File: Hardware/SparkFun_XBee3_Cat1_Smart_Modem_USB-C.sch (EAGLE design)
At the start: 53 parts, among them J4 QWIIC_RIGHT_ANGLE, U2 AP63203, U5 ESD Diode, U6 CP210X

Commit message: Moves parts around
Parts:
- removed FRAME2: FRAME-LETTER, SparkFun-Aesthetics:FRAME-LETTER
- added FRAME1: FRAME-LEDGER, SparkFun-Aesthetics:FRAME-LEDGER
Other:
- moved on the sheet: ALED, C1, C10, C2, C3, C4, C5, C6, C7, C8, C9, D2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

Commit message: Routes board
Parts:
- J3: value (none) -> USB Female Type C Connector; device SparkFun-Connectors:USB_C_2-LAYER_PADS -> SparkFun-Connectors:USB_C_4-LAYER-ISOLATED
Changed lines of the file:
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@@
 <part name="GND17" library="SparkFun-PowerSymbols" deviceset="GND" device=""/>
 <part name="J7" library="SparkFun-Connectors" deviceset="CONN_02" device="1X02_NO_SILK"/>
-<part name="J3" library="SparkFun-Connectors" deviceset="USB_C" device="_2-LAYER_PADS"/>
+<part name="J3" library="SparkFun-Connectors" deviceset="USB_C" device="_4-LAYER-ISOLATED" value="USB Female Type C Connector"/>
 <part name="GND4" library="SparkFun-PowerSymbols" deviceset="GND" device=""/>
 <part name="R7" library="SparkFun-Resistors" deviceset="5.1KOHM" device="5.1KOHM-0603-1/10W-1%" value="5.1k"/>

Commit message: Commits (finally) to shrinking the LED resistors so that I can fit in labels
* Increases schematic frame size to Ledger
* Adds measures
* Adds additional silk
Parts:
- LOGO3: value QWIIC_LOGO_5MM -> QWIIC_LOGO_3MM; device SparkFun-Aesthetics:QWIIC_LOGO_5MM -> SparkFun-Aesthetics:QWIIC_LOGO_3MM
- R11: device SparkFun-Resistors:1KOHM-0603-1/10W-1% -> SparkFun-Resistors:1KOHM-0402T-1/16W-1%
- R12, R2: device SparkFun-Resistors:2.2KOHM-0603-1/10W-1% -> SparkFun-Resistors:2.2KOHM-0402T-1/16W-1%
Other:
- note added: "Cut SHLD jumper to disconnect USB Shield from Ground."
- note added: "USB to UART - CP2104/2N"
- note added: "USB-C"
- note removed: "Cut SHLD/SHLD1 jumper to disconnect USB Shields from Ground."
- moved on the sheet: ALED, C1, C10, C2, C3, C4, C5, C6, C7, C8, C9, D2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

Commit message: Replaces UART IC
* Cuts back ground pour to make room for smaller modules RF singnals
* Fixes polygons
* Adds yellow LED
* Adds additional decoupling caps for RF board
* Increases the size of the board by 0.1" to make space for decoupling caps
* Updates the inductor for switching regulator
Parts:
- removed J7: (no value), SparkFun-Connectors:CONN_021X02_NO_SILK
- removed R17: 22k, SparkFun-Resistors:22KOHM-0603-1/10W-1%
- removed R18: 33k, SparkFun-Resistors:33KOHM-0603-1/10W-1%
- removed R9: 10k, SparkFun-Resistors:10KOHM-0603-1/10W-1%
- removed U6: CP210X, SparkFun-IC-Comms:CP2102N
- added C11, C14: 0.1uF, SparkFun-Capacitors:0.1UF-0603-25V-(+80/-20%)
- added J1, J8: (no value), SparkFun-Connectors:CONN_01PTH_NO_SILK_STAND
- added JP1: (no value), SparkFun-RF:XBEESMD
- added U7: FT231XS, SparkFun-IC-Comms:FT231XS
- C5: value 0.1uF -> 47pF; device SparkFun-Capacitors:0.1UF-0603-25V-(+80/-20%) -> SparkFun-Capacitors:47PF-0603-50V-5%
- C8: value 4.7uF -> 10pF; device SparkFun-Capacitors:4.7UF-0603-6.3V-(10%) -> SparkFun-Capacitors:10PF-0603-50V-5%
- D2: value RED -> Red; device SparkFun-LED:LED-RED0603 -> SparkFun-LED:LED-RED-0603-WE
- D4: value BLUE -> Yellow; device SparkFun-LED:LED-BLUE0603 -> SparkFun-LED:LED-YELLOW0603
- L1: value 4.7μH -> 3.9UH; device SparkFun-Coils:4.7μH_SHIELDED_INDUCTORNPIS_LS -> SparkFun-Coils:3.9UH
- R11: value 1k -> 4.7k; device SparkFun-Resistors:1KOHM-0402T-1/16W-1% -> SparkFun-Resistors:4.7KOHM-0402T-1/16W-1%
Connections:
- removed net N$10: R17.1, R18.2, U6.VBUS
- removed net N$4: J2.D-
- removed net N$9: R9.2, U6.!RSTB
- net 3.3V: now also C11.1, C14.1, U7.!RESET, U7.3V3OUT, U7.VCC, U7.VCCIO; no longer R9.1, U6.VDD, U6.VIO, U6.VREGIN
- net D+: now also U7.USBDP; no longer U6.D+
- net D-: now also U7.USBDM; no longer U6.D-
- net D13/TXO: now also U7.RXD; no longer U6.RXD
- net D14/RXI: now also U7.TXD; no longer U6.TXD
- net D6/!RTS!: now also U7.!RTS; no longer U6.RTS
- net D7/!CTS!: now also U7.!CTS
- net D8/!DTR!: now also U7.!DTR; no longer U6.DTR
- net EN: now also J8.1; no longer J7.1
- net GND: now also C11.2, C14.2, U7.GND@16, U7.GND@6; no longer R18.1, U6.GND
- net VIN: now also J1.1; no longer J7.2, R17.2
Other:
- note added: "RF Module - XBee 3"
- note added: "USB to UART - FT231XS"
- note removed: "RF Module - XBee 3 Cat 1 Smart Modem"
- note removed: "USB to UART - CP2104/2N"
- moved on the sheet: C5, C7, C8, C9

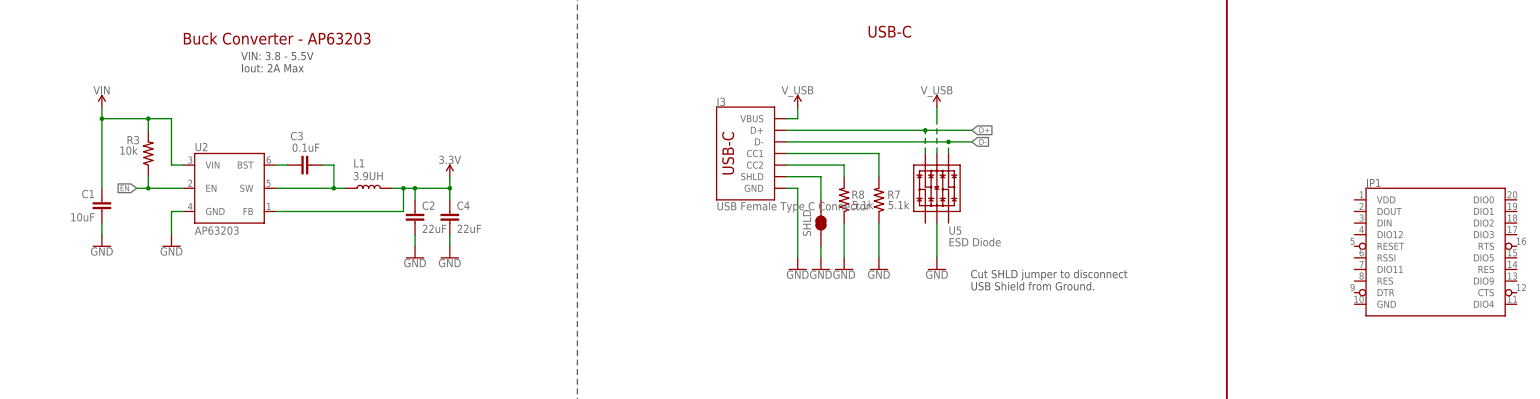
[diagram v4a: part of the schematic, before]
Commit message: Routes some airwires
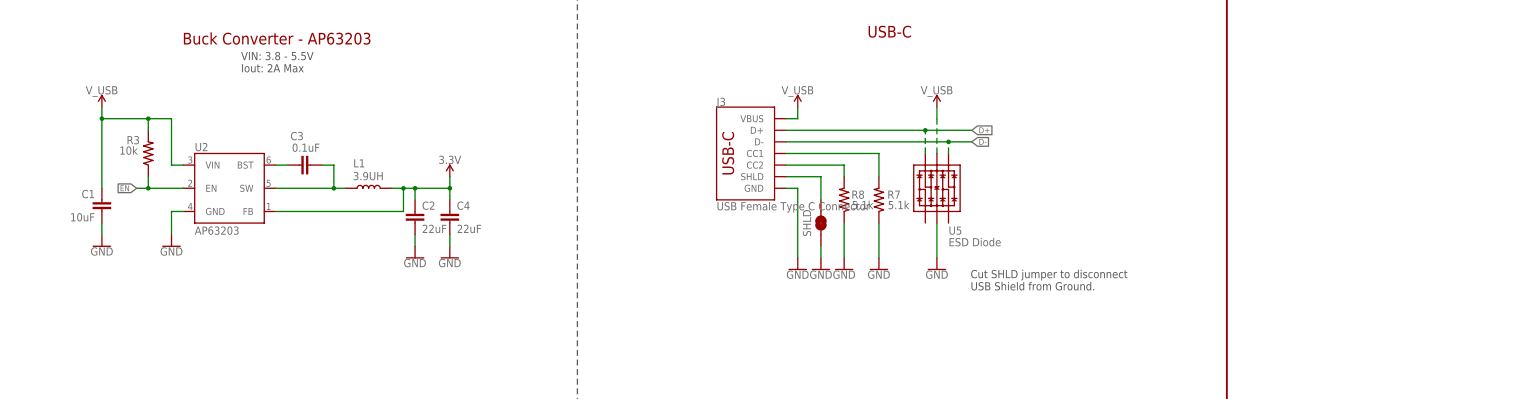
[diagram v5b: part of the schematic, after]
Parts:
- removed JP1: (no value), SparkFun-RF:XBEESMD
- J2: device xbee_smart_modem:XBEE_UPDATEXBEE_SMD_SILK -> xbee_smart_modem:XBEE_UPDATEXBEE_SMD
- R11: device SparkFun-Resistors:4.7KOHM-0402T-1/16W-1% -> SparkFun-Resistors:4.7KOHM-0603-1/10W-1%
- R12, R2: device SparkFun-Resistors:2.2KOHM-0402T-1/16W-1% -> SparkFun-Resistors:2.2KOHM-0603-1/10W-1%
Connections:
- net VIN: no longer C1.1, R3.2, U2.VIN
- net V_USB: now also C1.1, R3.2, U2.VIN

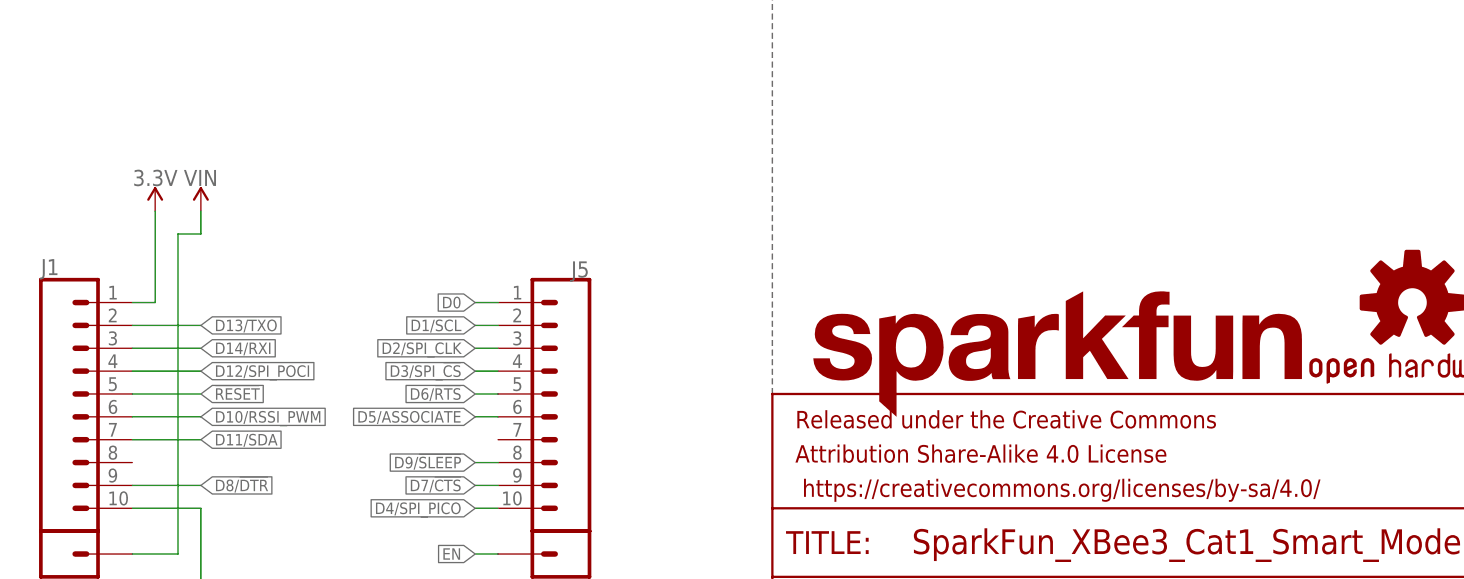
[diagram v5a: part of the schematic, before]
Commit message: Finishes routing airwires, fixes silk
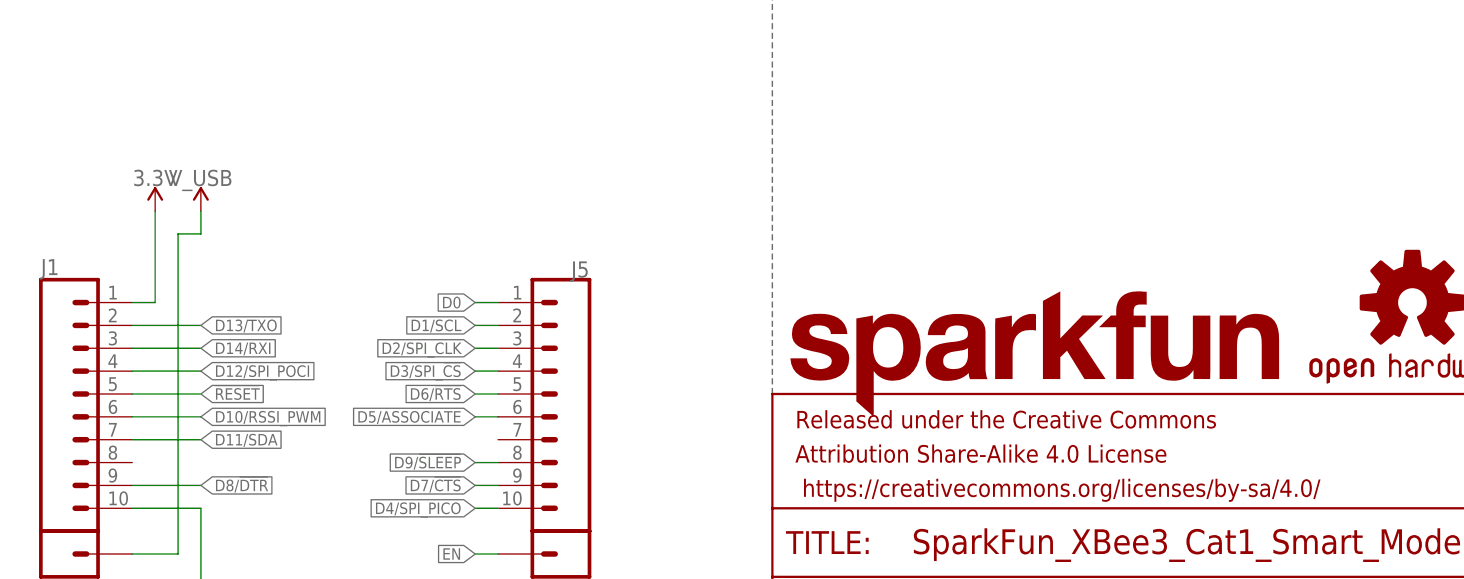
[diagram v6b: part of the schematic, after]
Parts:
- LOGO1: value SFE_LOGO_NAME.1_INCH -> SFE_LOGO_NAME.2_INCH; device SparkFun-Aesthetics:SFE_LOGO_NAME.1_INCH -> SparkFun-Aesthetics:SFE_LOGO_NAME.2_INCH
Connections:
- removed net VIN: J1.1
- net V_USB: now also J1.1
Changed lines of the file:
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@@
 <part name="PLED" library="SparkFun-Jumpers" deviceset="JUMPER-SMT_2_NC_TRACE" device="_SILK" package3d_urn="urn:adsk.eagle:package:39281/1"/>
 <part name="ALED" library="SparkFun-Jumpers" deviceset="JUMPER-SMT_2_NC_TRACE" device="_SILK" package3d_urn="urn:adsk.eagle:package:39281/1"/>
-<part name="LOGO1" library="SparkFun-Aesthetics" deviceset="SFE_LOGO_NAME" device=".1_INCH" value="SFE_LOGO_NAME.1_INCH"/>
 <part name="LOGO2" library="SparkFun-Aesthetics" deviceset="OSHW-LOGO" device="S"/>
 <part name="LOGO3" library="SparkFun-Aesthetics" deviceset="QWIIC_LOGO" device="_3MM" value="QWIIC_LOGO_3MM"/>
@@
 <part name="J1" library="SparkFun-Connectors" deviceset="CONN_01" device="PTH_NO_SILK_STAND"/>
 <part name="J8" library="SparkFun-Connectors" deviceset="CONN_01" device="PTH_NO_SILK_STAND"/>
-<part name="SUPPLY12" library="SparkFun-PowerSymbols" deviceset="VIN" device=""/>
 <part name="SUPPLY5" library="SparkFun-PowerSymbols" deviceset="V_USB" device=""/>
+<part name="SUPPLY11" library="SparkFun-PowerSymbols" deviceset="V_USB" device=""/>
+<part name="LOGO1" library="SparkFun-Aesthetics" deviceset="SFE_LOGO_NAME" device=".2_INCH"/>
 </parts>
 <sheets>
@@
 <attribute name="NAME" x="187.96" y="93.472" size="1.778" layer="95" font="vector" rot="R180" align="center"/>
 </instance>
-<instance part="LOGO1" gate="G$1" x="332.74" y="33.02" smashed="yes"/>
 <instance part="LOGO2" gate="G$1" x="401.32" y="45.72" smashed="yes"/>
 <instance part="LOGO3" gate="G$1" x="421.64" y="40.64" smashed="yes"/>
@@
 <attribute name="NAME" x="309.88" y="14.732" size="1.778" layer="95" font="vector" rot="R180"/>
 </instance>
-<instance part="SUPPLY12" gate="G$1" x="266.7" y="55.88" smashed="yes">
-<attribute name="VALUE" x="266.7" y="58.674" size="1.778" layer="96" font="vector" align="bottom-center"/>
-</instance>
 <instance part="SUPPLY5" gate="G$1" x="185.42" y="246.38" smashed="yes">
 <attribute name="VALUE" x="185.42" y="249.174" size="1.778" layer="96" font="vector" align="bottom-center"/>
 </instance>
+<instance part="SUPPLY11" gate="G$1" x="266.7" y="55.88" smashed="yes">
+<attribute name="VALUE" x="266.7" y="58.674" size="1.778" layer="96" font="vector" align="bottom-center"/>
+</instance>
+<instance part="LOGO1" gate="G$1" x="330.2" y="33.02" smashed="yes"/>
 </instances>
 <busses>
@@
 </segment>
 </net>
-<net name="VIN" class="0">
-<segment>
-<wire x1="259.08" y1="17.78" x2="264.16" y2="17.78" width="0.1524" layer="91"/>
-<wire x1="264.16" y1="17.78" x2="264.16" y2="53.34" width="0.1524" layer="91"/>
-<pinref part="J1" gate="G$1" pin="1"/>
-<wire x1="264.16" y1="53.34" x2="266.7" y2="53.34" width="0.1524" layer="91"/>
-<wire x1="266.7" y1="53.34" x2="266.7" y2="55.88" width="0.1524" layer="91"/>
-<pinref part="SUPPLY12" gate="G$1" pin="VIN"/>
-</segment>
-</net>
 <net name="N$21" class="0">
 <segment>
@@
 <pinref part="SUPPLY5" gate="G$1" pin="V_USB"/>
 </segment>
-</net>
+<segment>
+<wire x1="259.08" y1="17.78" x2="264.16" y2="17.78" width="0.1524" layer="91"/>
+<wire x1="264.16" y1="17.78" x2="264.16" y2="53.34" width="0.1524" layer="91"/>
+<pinref part="J1" gate="G$1" pin="1"/>
+<wire x1="264.16" y1="53.34" x2="266.7" y2="53.34" width="0.1524" layer="91"/>
+<wire x1="266.7" y1="53.34" x2="266.7" y2="55.88" width="0.1524" layer="91"/>
+<pinref part="SUPPLY11" gate="G$1" pin="V_USB"/>
+</segment>
+</net>
